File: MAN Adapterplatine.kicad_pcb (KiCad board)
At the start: 2 copper layers, 64.6 x 36.8 mm, 14 parts, among them J1 Cable, J2 Module, SW1 Address, U1 74HC165

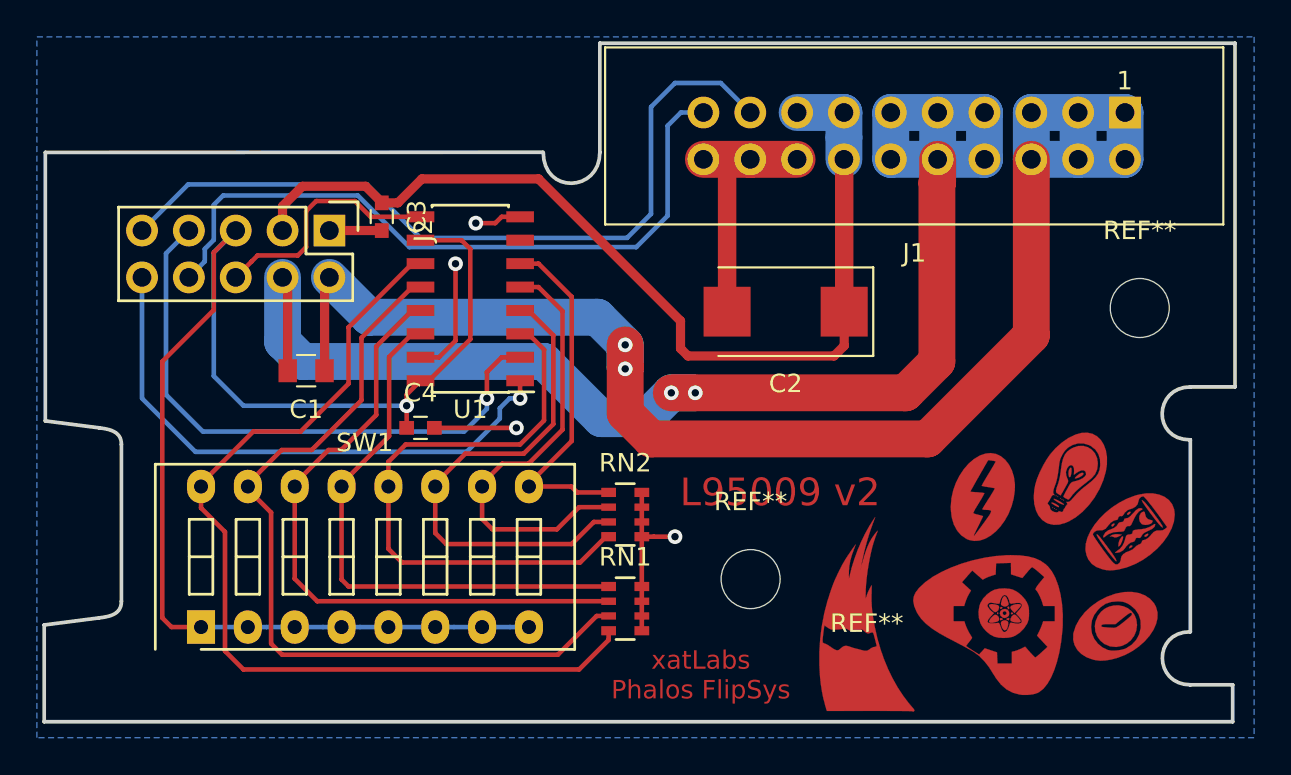
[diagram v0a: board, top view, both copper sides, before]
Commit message: Change DIP switch to include solder jumpers, add Elecrow data
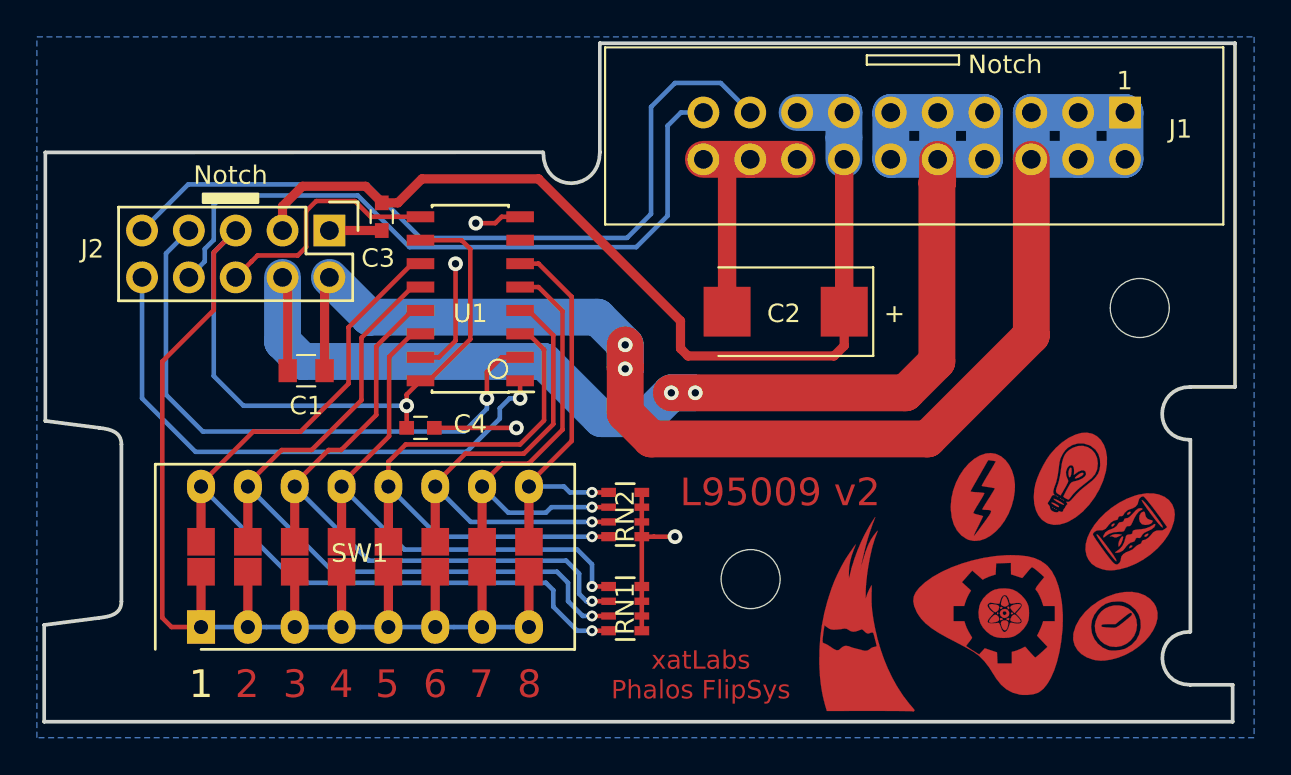
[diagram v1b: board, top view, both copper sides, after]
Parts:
- SW1: footprint Buttons_Switches_THT:SW_DIP_x8_Slide -> custom:SW_DIP_x8_Slide_SolderJumpers
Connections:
- U1 pad 7: Net-(U1-Pad7) -> unconnected-(U1-Pad7)
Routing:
- net Net-(RN1-Pad4): track 50.6 -> 44.6 mm, vias 0 -> 1
- net Net-(RN1-Pad3): track 44.4 -> 39.0 mm, vias 0 -> 1
- net Net-(RN2-Pad4): track 32.4 -> 29.3 mm, vias 0 -> 1
- net Net-(RN2-Pad3): track 27.7 -> 25.3 mm, vias 0 -> 1
- net Net-(RN1-Pad2): track 35.6 -> 33.3 mm, vias 0 -> 1
- net Net-(RN1-Pad1): track 30.0 -> 27.7 mm, vias 0 -> 1
- net Net-(RN2-Pad2): track 24.3 -> 22.6 mm, vias 0 -> 1
- net Net-(RN2-Pad1): vias 0 -> 1
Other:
- net class Default removed
- rule pad_to_mask_clearance: 0.051 -> 0
- board text added: "+"
- board text added: "1"
- board text added: "2"
- board text added: "3"
- board text added: "4"
- board text added: "5"
- board text added: "6"
- board text added: "7"
- board text added: "8"
- board text added: "Notch"
